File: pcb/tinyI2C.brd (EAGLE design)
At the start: 83.2 x 83.2 mm, 34 parts, among them IC1 74LVC1G125DCK, IC2 74LVC1G125DCK, IC3 IC_LDO_MIC5355, U1 LPC824M201JHI33, X1 TSW-112-02-S-S, X2 TSW-112-02-S-S, X3 TSW-106-02-S-S-RA, X4 TSW-102-02-S-S, X5 TSW-102-02-S-S, X6 TSW-102-02-S-S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

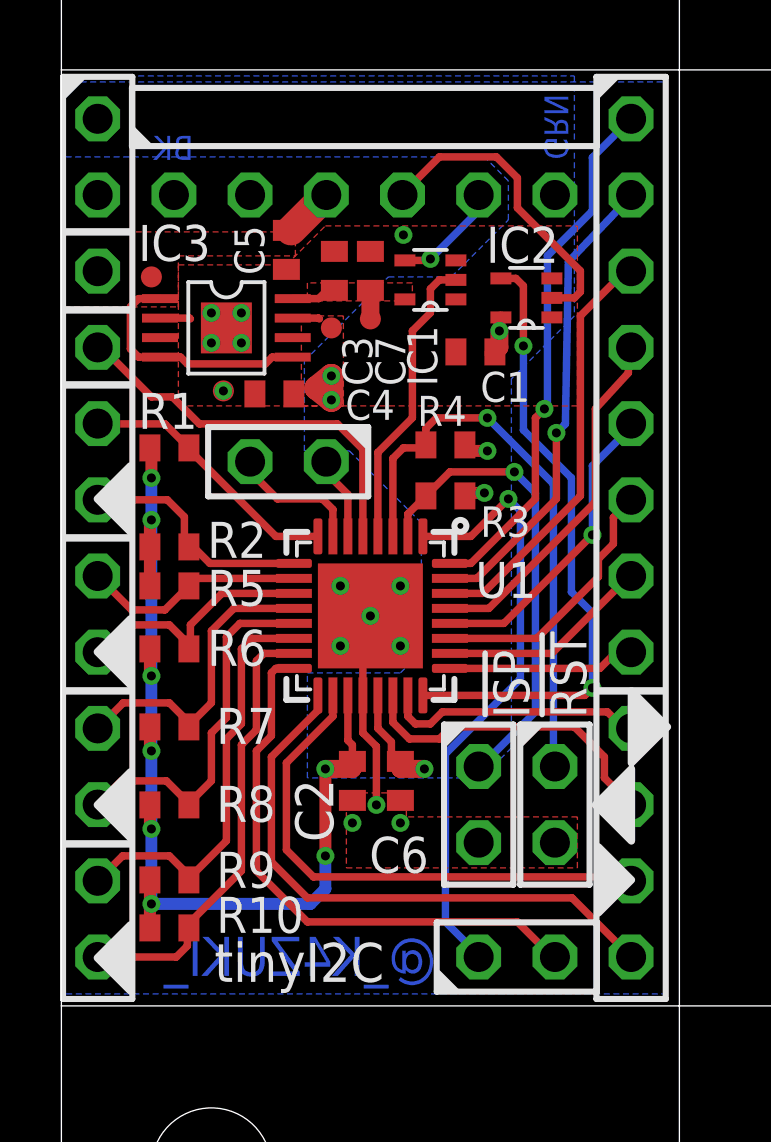
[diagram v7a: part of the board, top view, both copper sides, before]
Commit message: [ PCB ][ SCH ] replace as library did [ BRD ] I2C / SPI silk indicator
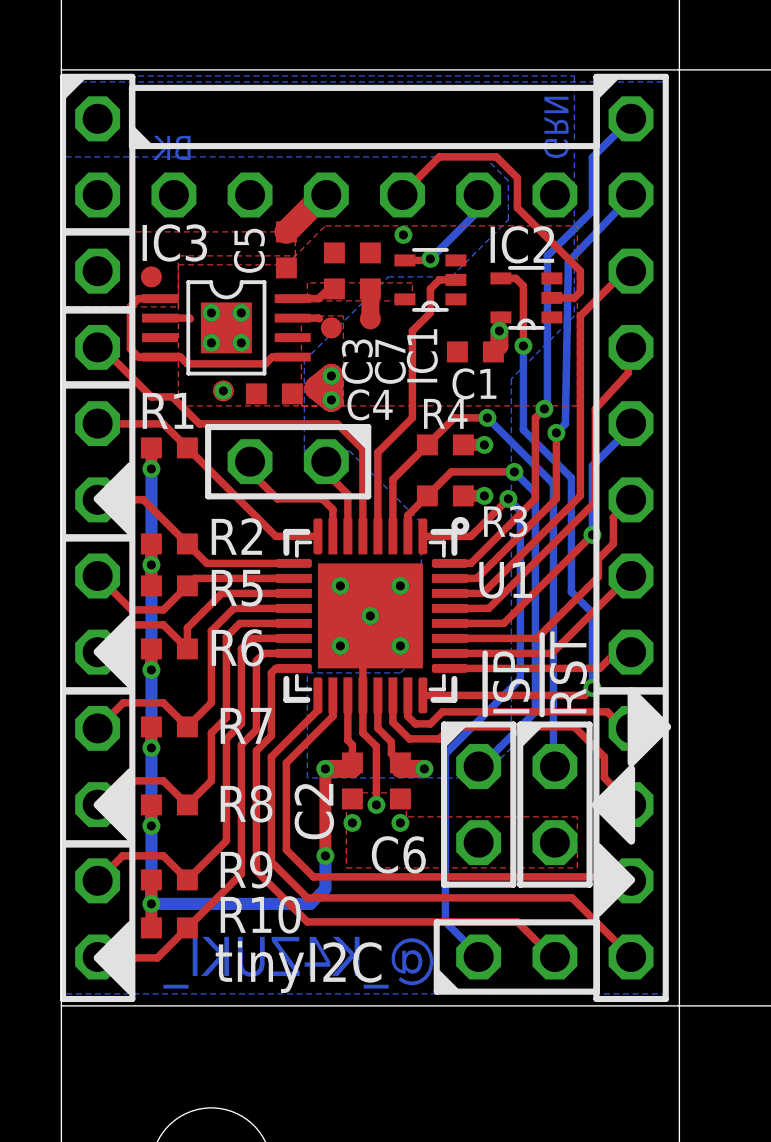
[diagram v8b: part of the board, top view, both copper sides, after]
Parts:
- TP1, TP2, TP3, TP6: device testpad:TP07R -> testpad_local:TP07R
- moved R2 0.10 mm to (3.60, 25.8)
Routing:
- net 1.8V: track 44.6 -> 42.9 mm
- net !RESET!: track 19.2 -> 18.5 mm
